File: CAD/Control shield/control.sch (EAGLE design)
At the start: 8 parts

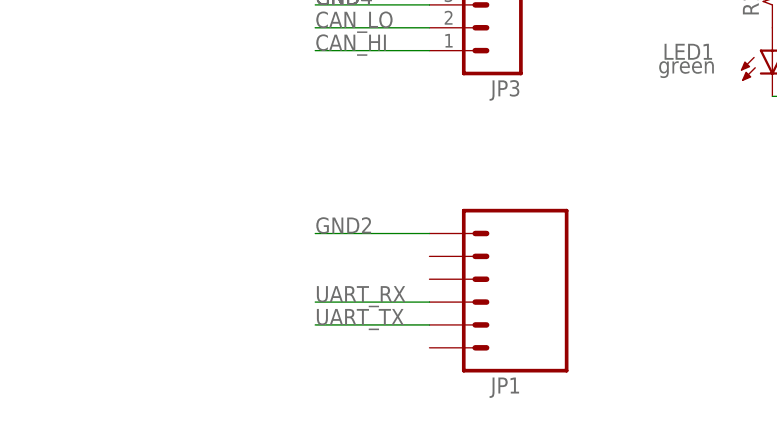
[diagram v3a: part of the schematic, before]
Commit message: Updated all CANode shields to fit the latest version of it.
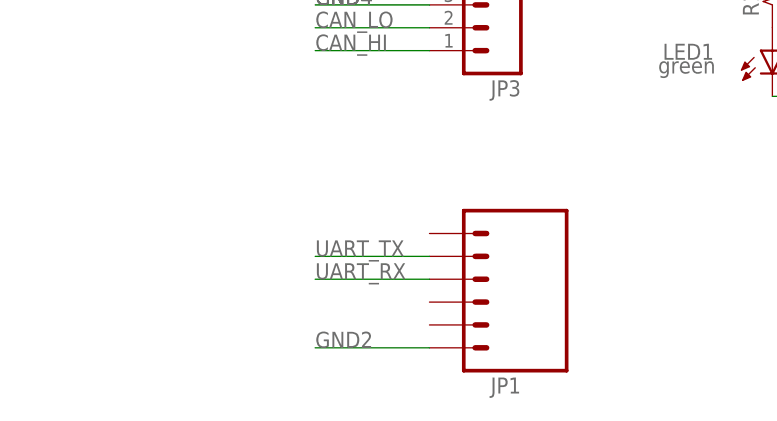
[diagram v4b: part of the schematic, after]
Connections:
- net GND2: now also JP1.1; no longer JP1.6
- net UART_RX: now also JP1.4; no longer JP1.3
- net UART_TX: now also JP1.5; no longer JP1.2
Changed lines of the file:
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@@
 </segment>
 <segment>
-<pinref part="JP1" gate="G$1" pin="6"/>
-<wire x1="68.58" y1="-5.08" x2="55.88" y2="-5.08" width="0.1524" layer="91"/>
-<label x="55.88" y="-5.08" size="1.778" layer="95"/>
+<pinref part="JP1" gate="G$1" pin="1"/>
+<wire x1="68.58" y1="-17.78" x2="55.88" y2="-17.78" width="0.1524" layer="91"/>
+<label x="55.88" y="-17.78" size="1.778" layer="95"/>
 </segment>
 </net>
@@
 <net name="UART_RX" class="0">
 <segment>
-<pinref part="JP1" gate="G$1" pin="3"/>
-<wire x1="68.58" y1="-12.7" x2="55.88" y2="-12.7" width="0.1524" layer="91"/>
-<label x="55.88" y="-12.7" size="1.778" layer="95"/>
-</segment>
-<segment>
 <pinref part="U$1" gate="G$1" pin="RB9"/>
 <wire x1="40.64" y1="43.18" x2="22.86" y2="43.18" width="0.1524" layer="91"/>
 <label x="22.86" y="43.18" size="1.778" layer="95"/>
 </segment>
+<segment>
+<pinref part="JP1" gate="G$1" pin="4"/>
+<wire x1="68.58" y1="-10.16" x2="55.88" y2="-10.16" width="0.1524" layer="91"/>
+<label x="55.88" y="-10.16" size="1.778" layer="95"/>
+</segment>
 </net>
 <net name="UART_TX" class="0">
-<segment>
-<pinref part="JP1" gate="G$1" pin="2"/>
-<wire x1="68.58" y1="-15.24" x2="55.88" y2="-15.24" width="0.1524" layer="91"/>
-<label x="55.88" y="-15.24" size="1.778" layer="95"/>
-</segment>
 <segment>
 <pinref part="U$1" gate="G$1" pin="RB8"/>
@@
 <label x="22.86" y="53.34" size="1.778" layer="95"/>
 </segment>
+<segment>
+<pinref part="JP1" gate="G$1" pin="5"/>
+<wire x1="68.58" y1="-7.62" x2="55.88" y2="-7.62" width="0.1524" layer="91"/>
+<label x="55.88" y="-7.62" size="1.778" layer="95"/>
+</segment>
 </net>
